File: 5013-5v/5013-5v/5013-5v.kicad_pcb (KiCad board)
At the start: 2 copper layers, 40 x 72 mm, 23 parts, among them IC1 LM5013DDAR

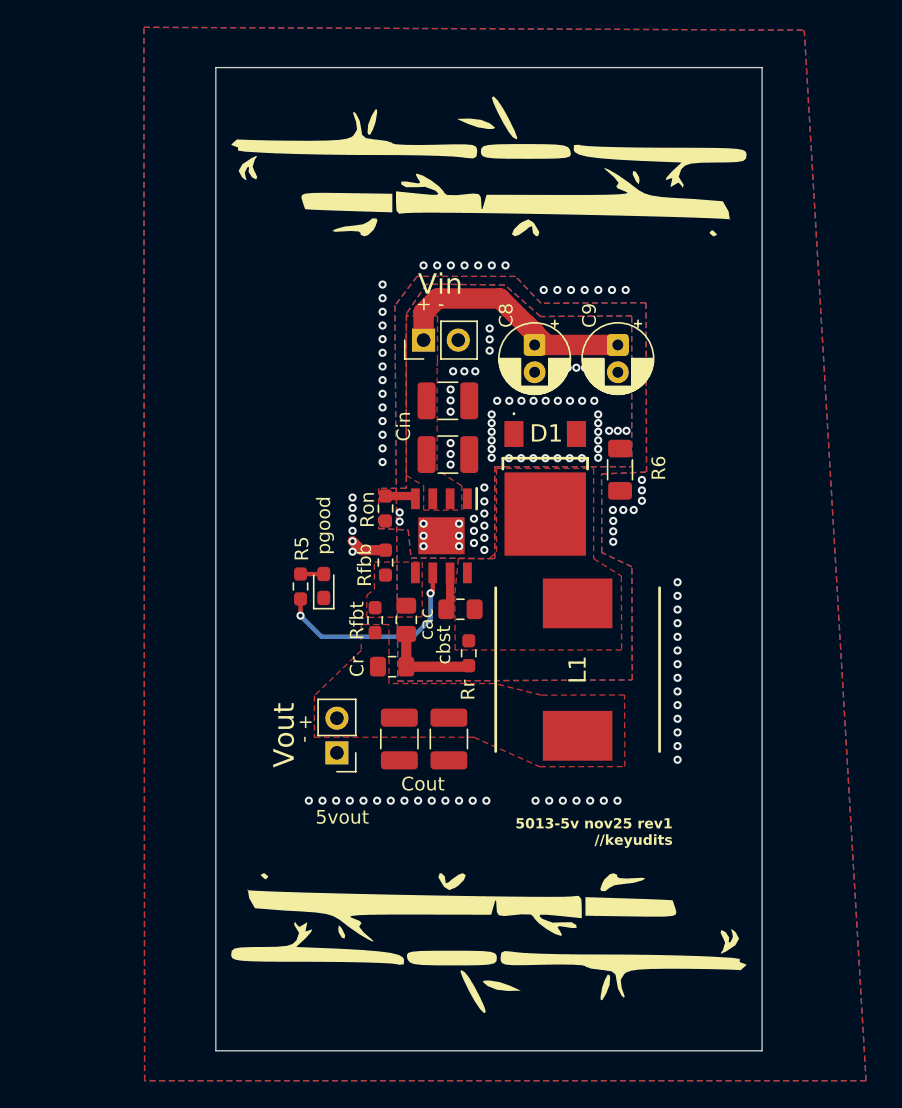
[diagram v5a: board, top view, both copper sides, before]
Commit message: began 5013-5v rev2 pcbnew
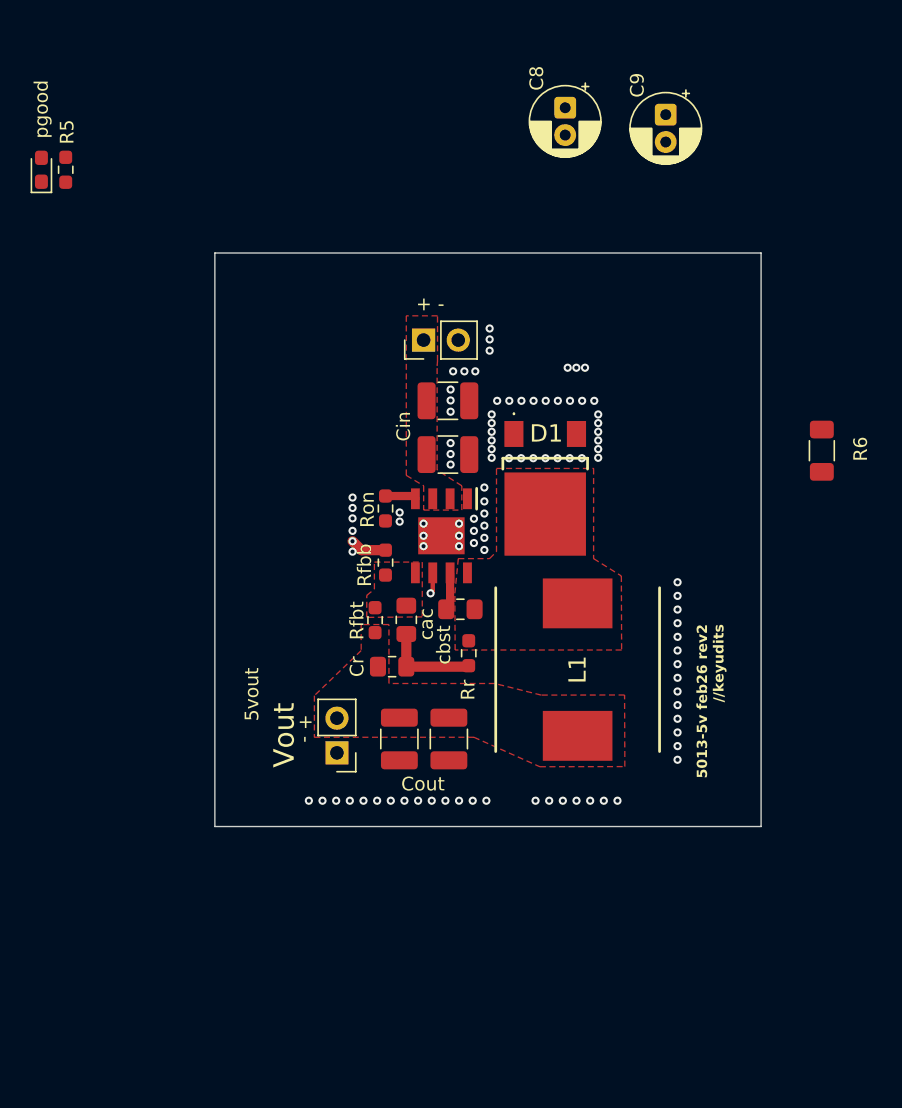
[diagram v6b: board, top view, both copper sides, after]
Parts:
- removed G*** (x2): LOGO, ear:nov25_4
- moved pgood 36.8 mm to (101.2, 69.3)
- moved R5 35.0 mm to (103.0, 69.3)
- moved C8 17.5 mm to (139.6, 64.7)
- moved C9 17.2 mm to (146.9, 65.2)
- moved R6 14.8 mm to (158.4, 89.9)
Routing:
- net /Vin: track 21.8 -> 0.00 mm
- net Net-(IC1-PGOOD): track 15.4 -> 1.57 mm, vias 2 -> 1
- net Net-(pgood1-A): track 1.70 -> 0.00 mm
- net GND1: vias 63 -> 60
- net GND: vias 78 -> 41
- removed copper zone on B.Cu, net GND
- removed copper zone on F.Cu, net GND
- removed copper zone on B.Cu, net GND1
- removed copper zone on F.Cu, net GND1
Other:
- board size 40 x 72 mm -> 40 x 42 mm
- board text added: "40x72mm 2mm safezone offset standard height DIN rail carrier *** 02/10/26 onhand: 40x42mm DIN rail carriers adjusting edgecuts"
- board text added: "5013-5v feb26 rev2 //keyudits"
- board text removed: "40x72mm 2mm safezone offset standard height DIN rail carrier"
- board text removed: "5013-5v nov25 rev1 //keyudits"
